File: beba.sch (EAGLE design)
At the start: 37 parts, among them IC1 LT1302SO08, IC2 MCP73871-2AAI/ML

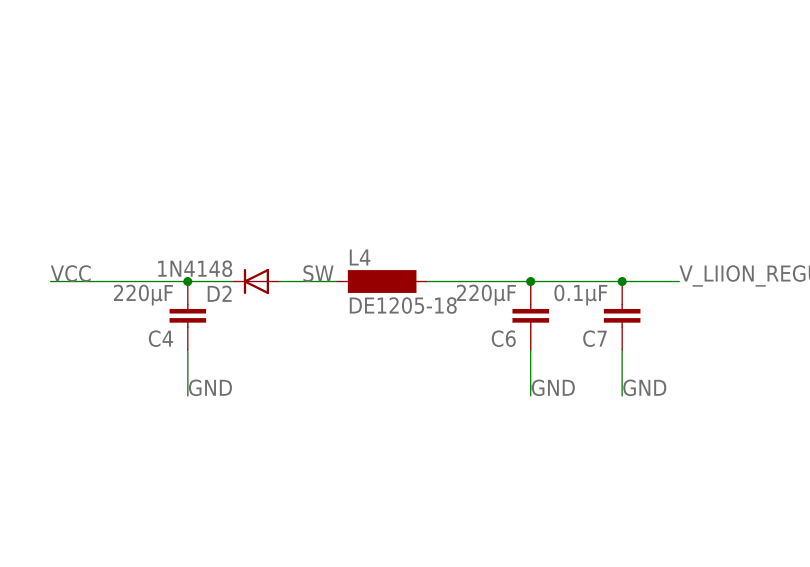
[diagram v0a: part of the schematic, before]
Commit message: - corrected issues with component placement, power inductor footprint, etc.
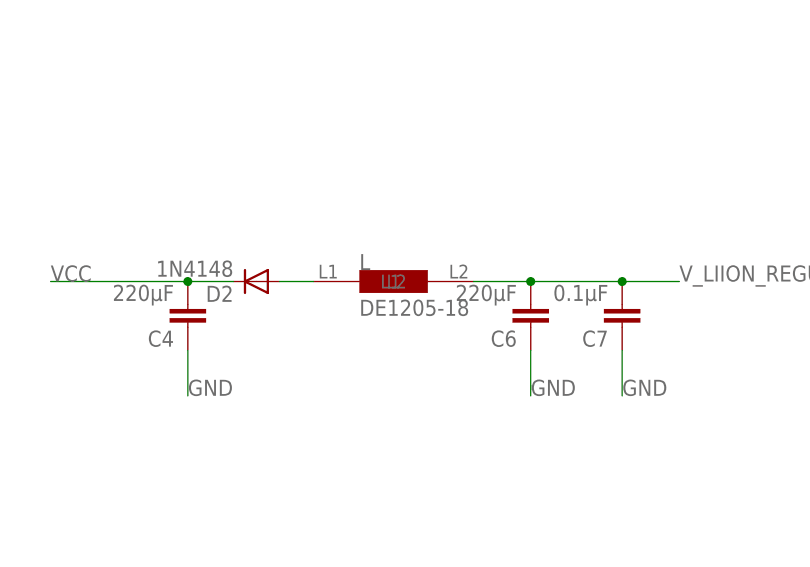
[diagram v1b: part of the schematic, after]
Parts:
- removed L4: DE1205-18, inductor-neosid:SM-1206
- added L: DE1205-18, DE1205-18 Power Inductor:DE1205-18
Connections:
- new net N$4: D2.A, L.L1
- net SW: no longer D2.A, L4.1
- net V_LIION_REGULATED: now also L.L2; no longer L4.2
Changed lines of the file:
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@@
 <setting verticaltext="up"/>
 </settings>
-<grid distance="0.1" unitdist="inch" unit="inch" style="lines" multiple="1" display="no" altdistance="0.01" altunitdist="inch" altunit="inch"/>
+<grid distance="0.1" unitdist="inch" unit="inch" style="lines" multiple="1" display="yes" altdistance="0.01" altunitdist="inch" altunit="inch"/>
 <layers>
 <layer number="1" name="Top" color="4" fill="1" visible="no" active="no"/>
@@
 <part name="C8" library="resistor" deviceset="C-EU" device="C0805" value="10μF"/>
 <part name="S1" library="smd-special" deviceset="SWS001" device="" value="POWER"/>
-<part name="L4" library="inductor-neosid" deviceset="SM-1206" device="" value="DE1205-18"/>
 <part name="CONN4" library="1734366-1 USB-A socket, vertical" deviceset="USB-A" device="" value="USB-A female socket, right angle"/>
 <part name="C9" library="rcl" deviceset="CPOL-EU" device="E2,5-6E" value="4700μF / 10V"/>
+<part name="L" library="DE1205-18 Power Inductor" deviceset="DE1205-18" device=""/>
 </parts>
 <sheets>
@@
 <instance part="C8" gate="G$1" x="299.72" y="151.13" rot="R180"/>
 <instance part="S1" gate="G$1" x="130.81" y="21.59" rot="R90"/>
-<instance part="L4" gate="G$1" x="71.12" y="115.57"/>
 <instance part="CONN4" gate="G$1" x="50.8" y="165.1"/>
 <instance part="C9" gate="G$1" x="319.532" y="151.13" rot="R180"/>
+<instance part="L" gate="G$1" x="73.66" y="114.3"/>
 </instances>
 <busses>
@@
 <wire x1="97.79" y1="115.57" x2="104.14" y2="115.57" width="0.1524" layer="91"/>
 <junction x="97.79" y="115.57"/>
-<pinref part="L4" gate="G$1" pin="2"/>
-<wire x1="87.63" y1="115.57" x2="76.2" y2="115.57" width="0.1524" layer="91"/>
+<pinref part="L" gate="G$1" pin="L2"/>
+<wire x1="81.28" y1="115.57" x2="87.63" y2="115.57" width="0.1524" layer="91"/>
 <junction x="87.63" y="115.57"/>
 </segment>
@@
 <label x="90.17" y="21.59" size="1.778" layer="95"/>
 </segment>
-<segment>
-<pinref part="D2" gate="1" pin="A"/>
-<wire x1="59.69" y1="115.57" x2="66.04" y2="115.57" width="0.1524" layer="91"/>
-<label x="62.23" y="115.57" size="1.778" layer="95"/>
-<pinref part="L4" gate="G$1" pin="1"/>
-</segment>
 </net>
 <net name="IT" class="2">
@@
 </segment>
 </net>
+<net name="N$4" class="0">
+<segment>
+<pinref part="D2" gate="1" pin="A"/>
+<pinref part="L" gate="G$1" pin="L1"/>
+<wire x1="59.69" y1="115.57" x2="63.5" y2="115.57" width="0.1524" layer="91"/>
+</segment>
+</net>

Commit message: - further minor corrections
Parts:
- added 5V0, VLIION: PTR1B2,54, testpad:PTR1B2,54
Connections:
- net 5V0: now also 5V0.TP
- net V_LIION_REGULATED: now also VLIION.TP
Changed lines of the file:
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@@
 <grid distance="0.1" unitdist="inch" unit="inch" style="lines" multiple="1" display="yes" altdistance="0.01" altunitdist="inch" altunit="inch"/>
 <layers>
-<layer number="1" name="Top" color="4" fill="1" visible="no" active="no"/>
-<layer number="2" name="Route2" color="1" fill="3" visible="no" active="no"/>
-<layer number="3" name="Route3" color="4" fill="3" visible="no" active="no"/>
-<layer number="4" name="Route4" color="1" fill="4" visible="no" active="no"/>
-<layer number="5" name="Route5" color="4" fill="4" visible="no" active="no"/>
-<layer number="6" name="Route6" color="1" fill="8" visible="no" active="no"/>
-<layer number="7" name="Route7" color="4" fill="8" visible="no" active="no"/>
-<layer number="8" name="Route8" color="1" fill="2" visible="no" active="no"/>
-<layer number="9" name="Route9" color="4" fill="2" visible="no" active="no"/>
-<layer number="10" name="Route10" color="1" fill="7" visible="no" active="no"/>
-<layer number="11" name="Route11" color="4" fill="7" visible="no" active="no"/>
-<layer number="12" name="Route12" color="1" fill="5" visible="no" active="no"/>
-<layer number="13" name="Route13" color="4" fill="5" visible="no" active="no"/>
-<layer number="14" name="Route14" color="1" fill="6" visible="no" active="no"/>
-<layer number="15" name="Route15" color="4" fill="6" visible="no" active="no"/>
-<layer number="16" name="Bottom" color="1" fill="1" visible="no" active="no"/>
-<layer number="17" name="Pads" color="2" fill="1" visible="no" active="no"/>
-<layer number="18" name="Vias" color="2" fill="1" visible="no" active="no"/>
-<layer number="19" name="Unrouted" color="6" fill="1" visible="no" active="no"/>
-<layer number="20" name="Dimension" color="15" fill="1" visible="no" active="no"/>
-<layer number="21" name="tPlace" color="7" fill="1" visible="no" active="no"/>
-<layer number="22" name="bPlace" color="7" fill="1" visible="no" active="no"/>
-<layer number="23" name="tOrigins" color="15" fill="1" visible="no" active="no"/>
-<layer number="24" name="bOrigins" color="15" fill="1" visible="no" active="no"/>
-<layer number="25" name="tNames" color="7" fill="1" visible="no" active="no"/>
-<layer number="26" name="bNames" color="7" fill="1" visible="no" active="no"/>
-<layer number="27" name="tValues" color="7" fill="1" visible="no" active="no"/>
-<layer number="28" name="bValues" color="7" fill="1" visible="no" active="no"/>
+<layer number="1" name="Top" color="4" fill="1" visible="yes" active="no"/>
+<layer number="2" name="Route2" color="1" fill="3" visible="yes" active="no"/>
+<layer number="3" name="Route3" color="4" fill="3" visible="yes" active="no"/>
+<layer number="4" name="Route4" color="1" fill="4" visible="yes" active="no"/>
+<layer number="5" name="Route5" color="4" fill="4" visible="yes" active="no"/>
+<layer number="6" name="Route6" color="1" fill="8" visible="yes" active="no"/>
+<layer number="7" name="Route7" color="4" fill="8" visible="yes" active="no"/>
+<layer number="8" name="Route8" color="1" fill="2" visible="yes" active="no"/>
+<layer number="9" name="Route9" color="4" fill="2" visible="yes" active="no"/>
+<layer number="10" name="Route10" color="1" fill="7" visible="yes" active="no"/>
+<layer number="11" name="Route11" color="4" fill="7" visible="yes" active="no"/>
+<layer number="12" name="Route12" color="1" fill="5" visible="yes" active="no"/>
+<layer number="13" name="Route13" color="4" fill="5" visible="yes" active="no"/>
+<layer number="14" name="Route14" color="1" fill="6" visible="yes" active="no"/>
+<layer number="15" name="Route15" color="4" fill="6" visible="yes" active="no"/>
+<layer number="16" name="Bottom" color="1" fill="1" visible="yes" active="no"/>
+<layer number="17" name="Pads" color="2" fill="1" visible="yes" active="no"/>
+<layer number="18" name="Vias" color="2" fill="1" visible="yes" active="no"/>
+<layer number="19" name="Unrouted" color="6" fill="1" visible="yes" active="no"/>
+<layer number="20" name="Dimension" color="15" fill="1" visible="yes" active="no"/>
+<layer number="21" name="tPlace" color="7" fill="1" visible="yes" active="no"/>
+<layer number="22" name="bPlace" color="7" fill="1" visible="yes" active="no"/>
+<layer number="23" name="tOrigins" color="15" fill="1" visible="yes" active="no"/>
+<layer number="24" name="bOrigins" color="15" fill="1" visible="yes" active="no"/>
+<layer number="25" name="tNames" color="7" fill="1" visible="yes" active="no"/>
+<layer number="26" name="bNames" color="7" fill="1" visible="yes" active="no"/>
+<layer number="27" name="tValues" color="7" fill="1" visible="yes" active="no"/>
+<layer number="28" name="bValues" color="7" fill="1" visible="yes" active="no"/>
 <layer number="29" name="tStop" color="7" fill="3" visible="no" active="no"/>
 <layer number="30" name="bStop" color="7" fill="6" visible="no" active="no"/>
@@
 <layer number="35" name="tGlue" color="7" fill="4" visible="no" active="no"/>
 <layer number="36" name="bGlue" color="7" fill="5" visible="no" active="no"/>
-<layer number="37" name="tTest" color="7" fill="1" visible="no" active="no"/>
-<layer number="38" name="bTest" color="7" fill="1" visible="no" active="no"/>
+<layer number="37" name="tTest" color="7" fill="1" visible="yes" active="no"/>
+<layer number="38" name="bTest" color="7" fill="1" visible="yes" active="no"/>
 <layer number="39" name="tKeepout" color="4" fill="11" visible="no" active="no"/>
 <layer number="40" name="bKeepout" color="1" fill="11" visible="no" active="no"/>
@@
 <layer number="44" name="Drills" color="7" fill="1" visible="no" active="no"/>
 <layer number="45" name="Holes" color="7" fill="1" visible="no" active="no"/>
-<layer number="46" name="Milling" color="3" fill="1" visible="no" active="no"/>
-<layer number="47" name="Measures" color="7" fill="1" visible="no" active="no"/>
-<layer number="48" name="Document" color="7" fill="1" visible="no" active="no"/>
-<layer number="49" name="Reference" color="7" fill="1" visible="no" active="no"/>
-<layer number="50" name="dxf" color="7" fill="1" visible="no" active="no"/>
-<layer number="51" name="tDocu" color="7" fill="1" visible="no" active="no"/>
-<layer number="52" name="bDocu" color="7" fill="1" visible="no" active="no"/>
-<layer number="53" name="tGND_GNDA" color="7" fill="9" visible="no" active="no"/>
-<layer number="54" name="bGND_GNDA" color="1" fill="9" visible="no" active="no"/>
-<layer number="56" name="wert" color="7" fill="1" visible="no" active="no"/>
-<layer number="57" name="tCAD" color="7" fill="1" visible="no" active="no"/>
-<layer number="59" name="tCarbon" color="7" fill="1" visible="no" active="no"/>
-<layer number="60" name="bCarbon" color="7" fill="1" visible="no" active="no"/>
+<layer number="46" name="Milling" color="3" fill="1" visible="yes" active="no"/>
+<layer number="47" name="Measures" color="7" fill="1" visible="yes" active="no"/>
+<layer number="48" name="Document" color="7" fill="1" visible="yes" active="no"/>
+<layer number="49" name="Reference" color="7" fill="1" visible="yes" active="no"/>
+<layer number="50" name="dxf" color="7" fill="1" visible="yes" active="no"/>
+<layer number="51" name="tDocu" color="7" fill="1" visible="yes" active="no"/>
+<layer number="52" name="bDocu" color="7" fill="1" visible="yes" active="no"/>
+<layer number="53" name="tGND_GNDA" color="7" fill="9" visible="yes" active="no"/>
+<layer number="54" name="bGND_GNDA" color="1" fill="9" visible="yes" active="no"/>
+<layer number="56" name="wert" color="7" fill="1" visible="yes" active="no"/>
+<layer number="57" name="tCAD" color="7" fill="1" visible="yes" active="no"/>
+<layer number="59" name="tCarbon" color="7" fill="1" visible="yes" active="no"/>
+<layer number="60" name="bCarbon" color="7" fill="1" visible="yes" active="no"/>
 <layer number="90" name="Modules" color="5" fill="1" visible="yes" active="yes"/>
 <layer number="91" name="Nets" color="2" fill="1" visible="yes" active="yes"/>
@@
 <part name="C9" library="rcl" deviceset="CPOL-EU" device="E2,5-6E" value="4700μF / 10V"/>
 <part name="L" library="DE1205-18 Power Inductor" deviceset="DE1205-18" device=""/>
+<part name="5V0" library="testpad" deviceset="PTR1" device="B2,54"/>
+<part name="VLIION" library="testpad" deviceset="PTR1" device="B2,54"/>
 </parts>
 <sheets>
@@
 <instance part="C9" gate="G$1" x="319.532" y="151.13" rot="R180"/>
 <instance part="L" gate="G$1" x="73.66" y="114.3"/>
+<instance part="5V0" gate="G$1" x="322.58" y="99.06" rot="R270"/>
+<instance part="VLIION" gate="G$1" x="322.58" y="88.9" rot="R270"/>
 </instances>
 <busses>
@@
 <wire x1="135.89" y1="21.59" x2="139.7" y2="21.59" width="0.1524" layer="91"/>
 <label x="139.7" y="21.59" size="1.778" layer="95"/>
+</segment>
+<segment>
+<pinref part="VLIION" gate="G$1" pin="TP"/>
+<wire x1="325.12" y1="88.9" x2="330.2" y2="88.9" width="0.1524" layer="91"/>
+<label x="330.2" y="88.9" size="1.778" layer="95"/>
 </segment>
 </net>
@@
 <label x="327.66" y="148.59" size="1.778" layer="95"/>
 </segment>
+<segment>
+<pinref part="5V0" gate="G$1" pin="TP"/>
+<wire x1="325.12" y1="99.06" x2="330.2" y2="99.06" width="0.1524" layer="91"/>
+<label x="330.2" y="99.06" size="1.778" layer="95"/>
+</segment>
 </net>
 <net name="STAT2" class="2">
@@
 </segment>
 </net>
-<net name="N$4" class="0">
+<net name="N$4" class="1">
 <segment>
 <pinref part="D2" gate="1" pin="A"/>

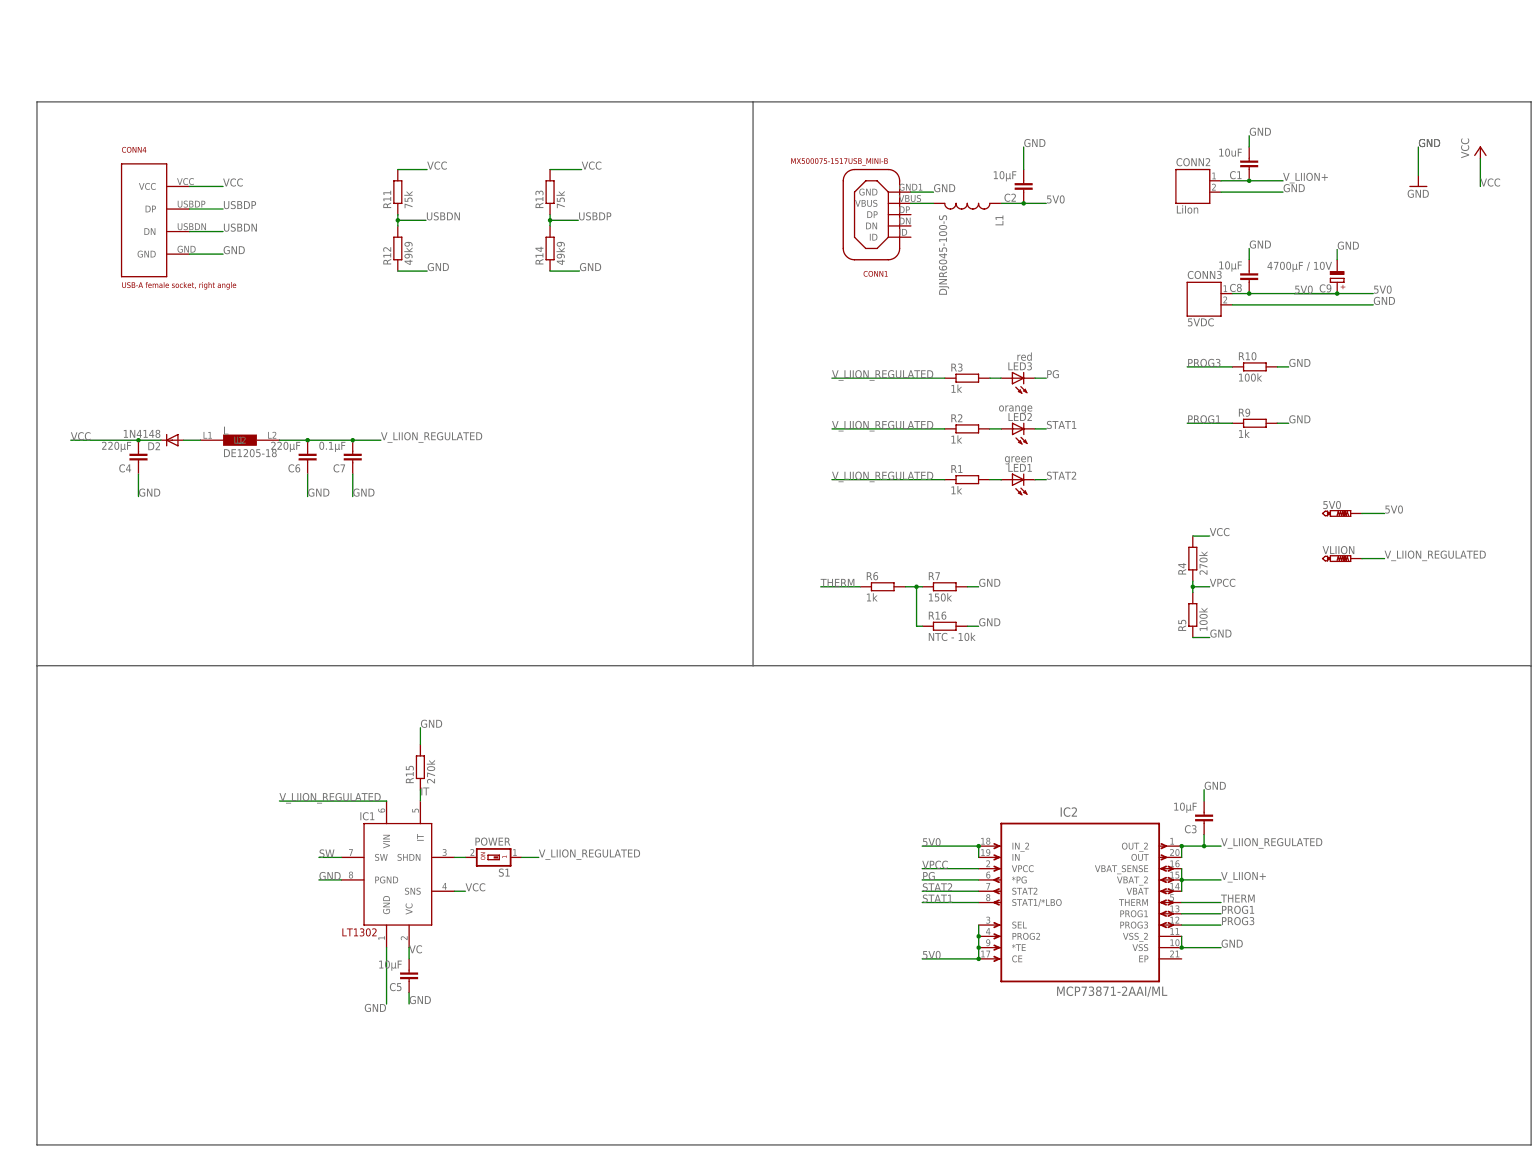
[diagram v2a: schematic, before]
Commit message: - minor corrections, added bom
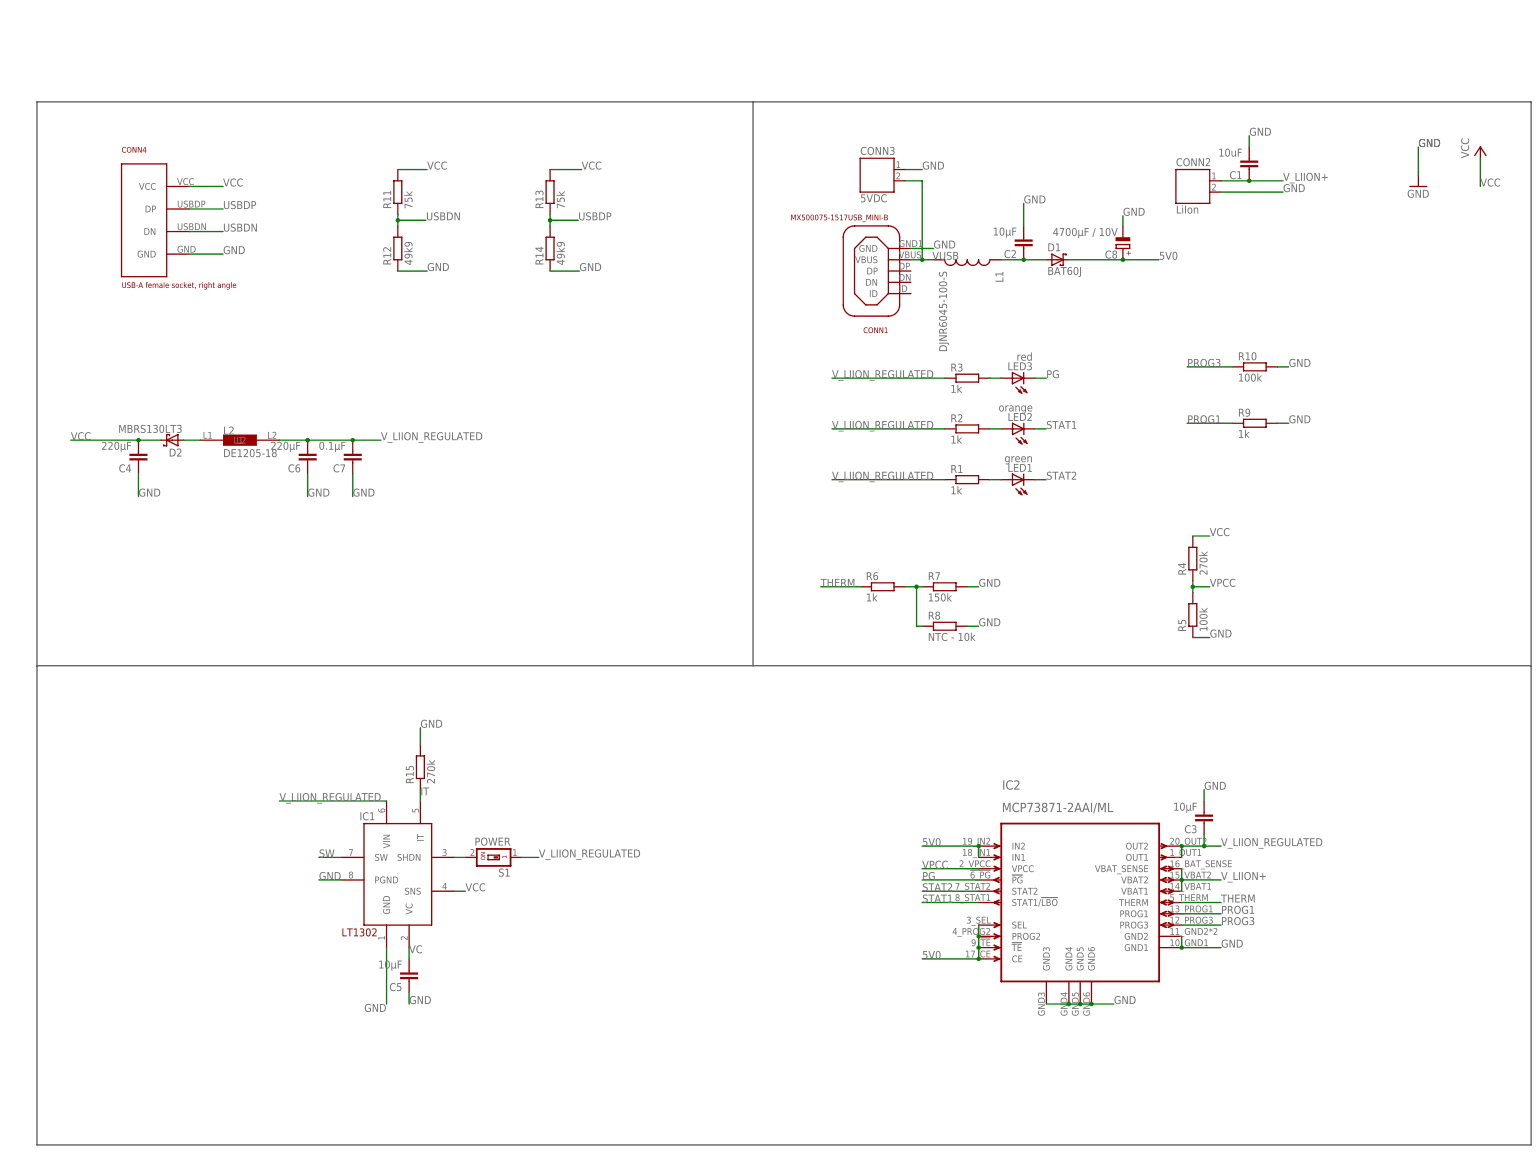
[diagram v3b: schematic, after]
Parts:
- removed 5V0, VLIION: PTR1B2,54, testpad:PTR1B2,54
- removed C9: 4700μF / 10V, rcl:CPOL-EUE2,5-6E
- added D1: BAT60J, diode:BAT60J
- C8: value 10μF -> 4700μF / 10V; device resistor:C-EUC0805 -> rcl:CPOL-EUE2,5-6E
- D2: value 1N4148 -> MBRS130LT3; device adafruit:1N4004 -> diode:MBRS130LT3
- IC2: device Microchip-MCP73871-2AAI_ML:MCP73871-2AAI/ML -> MCP73871 - Powerpath and Charge Controller:MCP73871-2AAI/ML
- renumbered L to L2, R16 to R8
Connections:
- net 5V0: now also C8.+, D1.A, D1.C, IC2.!TE!, IC2.IN1, IC2.IN2; no longer 5V0.TP, C8.1, C9.+, CONN3.1, IC2.*TE, IC2.IN, IC2.IN_2
- net GND: now also C8.-, CONN3.1, IC2.GND1, IC2.GND2, IC2.GND3, IC2.GND4, IC2.GND5, IC2.GND6; no longer C8.2, C9.-, CONN3.2, IC2.VSS, IC2.VSS_2
- net PG: now also IC2.!PG!; no longer IC2.*PG
- net STAT1: now also IC2.STAT1/!LBO!; no longer IC2.STAT1/*LBO
- net VUSB: now also CONN3.2
- net V_LIION+: now also IC2.VBAT1, IC2.VBAT2; no longer IC2.VBAT, IC2.VBAT_2
- net V_LIION_REGULATED: now also IC2.OUT1, IC2.OUT2; no longer IC2.OUT, IC2.OUT_2, VLIION.TP
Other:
- moved on the sheet: C2, CONN1, CONN3, L1
